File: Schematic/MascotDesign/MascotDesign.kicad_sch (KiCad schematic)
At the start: 10 parts, among them Q1 IRF540N

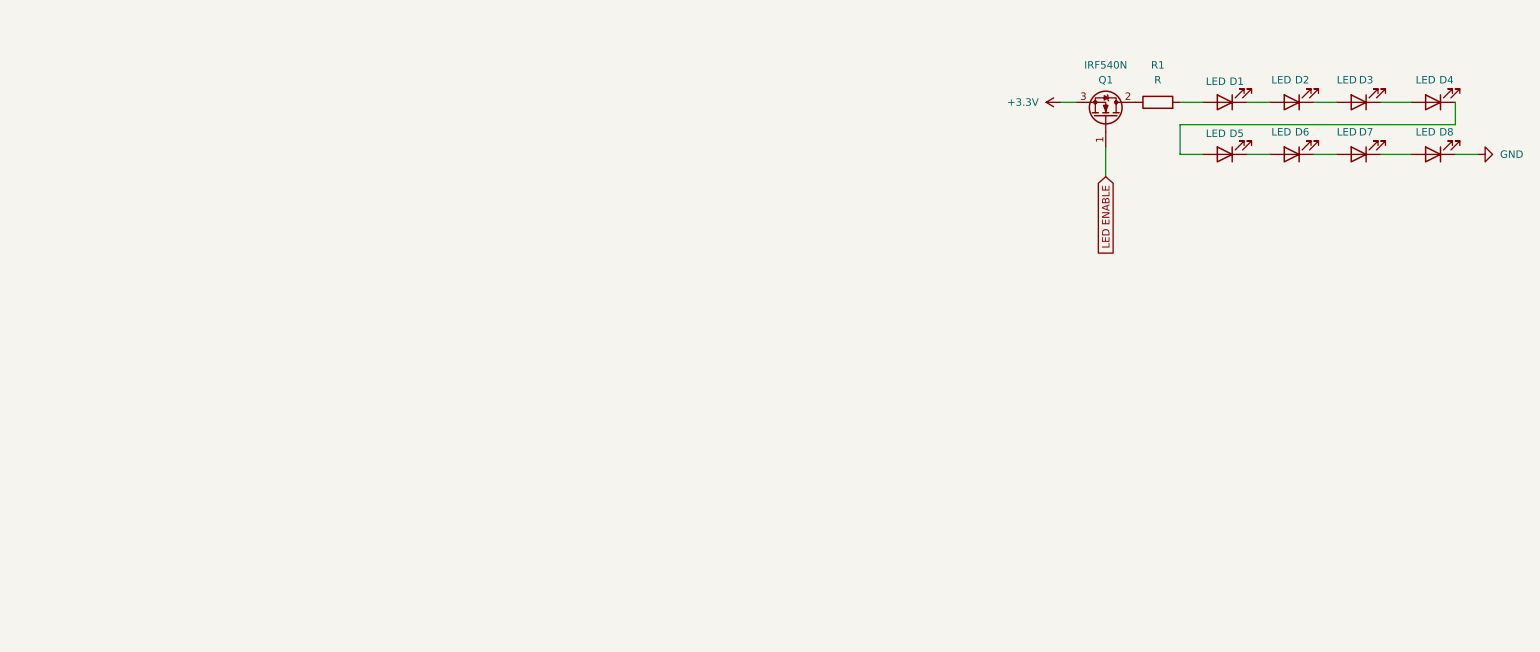
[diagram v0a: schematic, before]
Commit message: Work on schematic
create power module and LED module in the master sheet
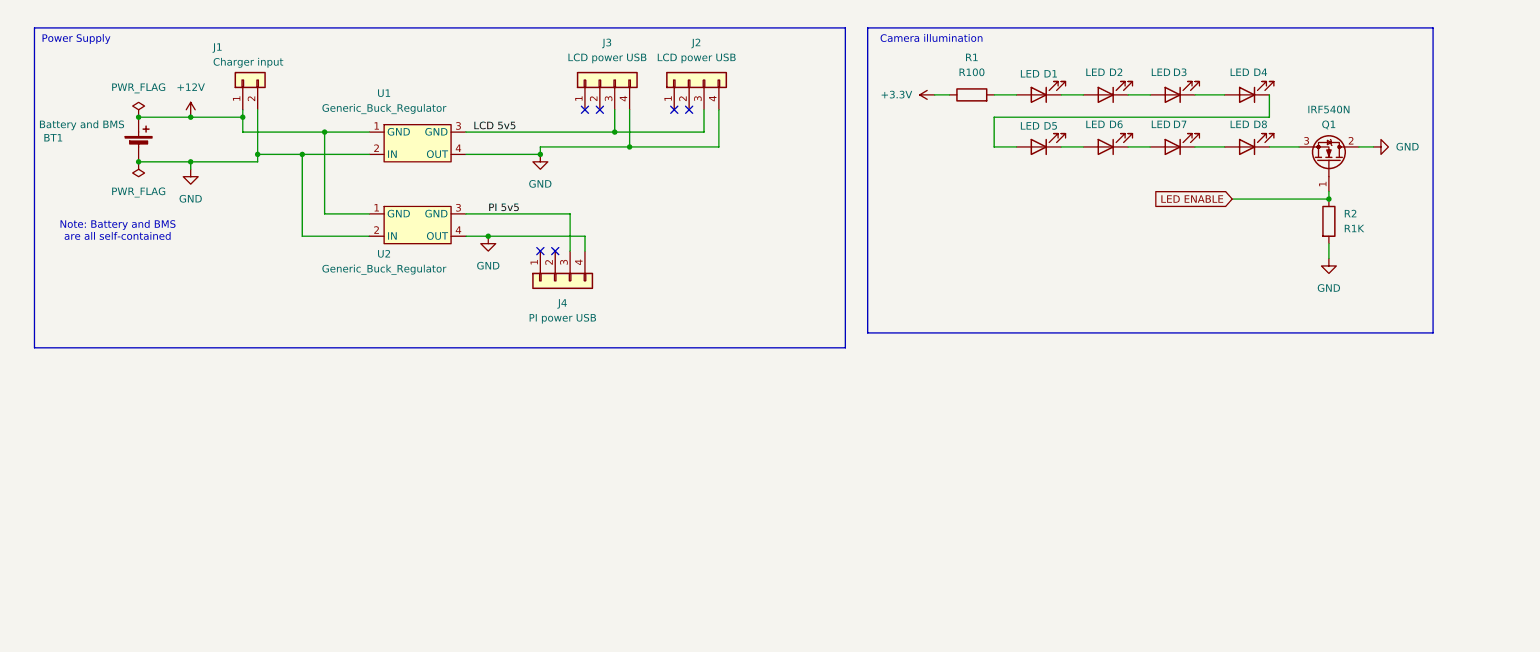
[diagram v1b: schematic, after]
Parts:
- added BT1: Battery and BMS, symbol Device:Battery_Cell
- added J1: Charger input, symbol Connector_Generic:Conn_01x02
- added J2, J3: LCD power USB, symbol Connector_Generic:Conn_01x04
- added J4: PI power USB, symbol Connector_Generic:Conn_01x04
- added R2: R1K, symbol Device:R
- added U1, U2: Generic_Buck_Regulator, My_Library:Generic Buck Regulator, symbol My_Library:Generic_Buck_Regulator
- R1: value R -> R100
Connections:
- net +3.3V: now also R1.1; no longer Q1.3 (S)
- net GND: now also Q1.2 (D), BT1.2 (-), J1.2 (Pin_2), J2.4 (Pin_4), J3.4 (Pin_4), J4.4 (Pin_4), R2.2, U1.2 (IN), U1.4 (OUT), U2.2 (IN), U2.4 (OUT); no longer D8.1 (K)
- net LED ENABLE: now also R2.1
- new net: D8.1 (K), Q1.3 (S)
- new net +12V: BT1.1 (+), J1.1 (Pin_1), U1.1 (GND), U2.1 (GND)
- new net LCD 5v5: J2.3 (Pin_3), J3.3 (Pin_3), U1.3 (GND)
- new net PI 5v5: J4.3 (Pin_3), U2.3 (GND)
- no-connect marks 0 -> 6
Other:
- note added: "Camera illumination"
- note added: "Note: Battery and BMS are all self-contained"
- note added: "Power Supply"
- moved on the sheet: D1, D2, D3, D4, D5, D6, D7, D8, Q1, R1

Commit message: organize PCB schematic into different files
so multiple people can edit different parts
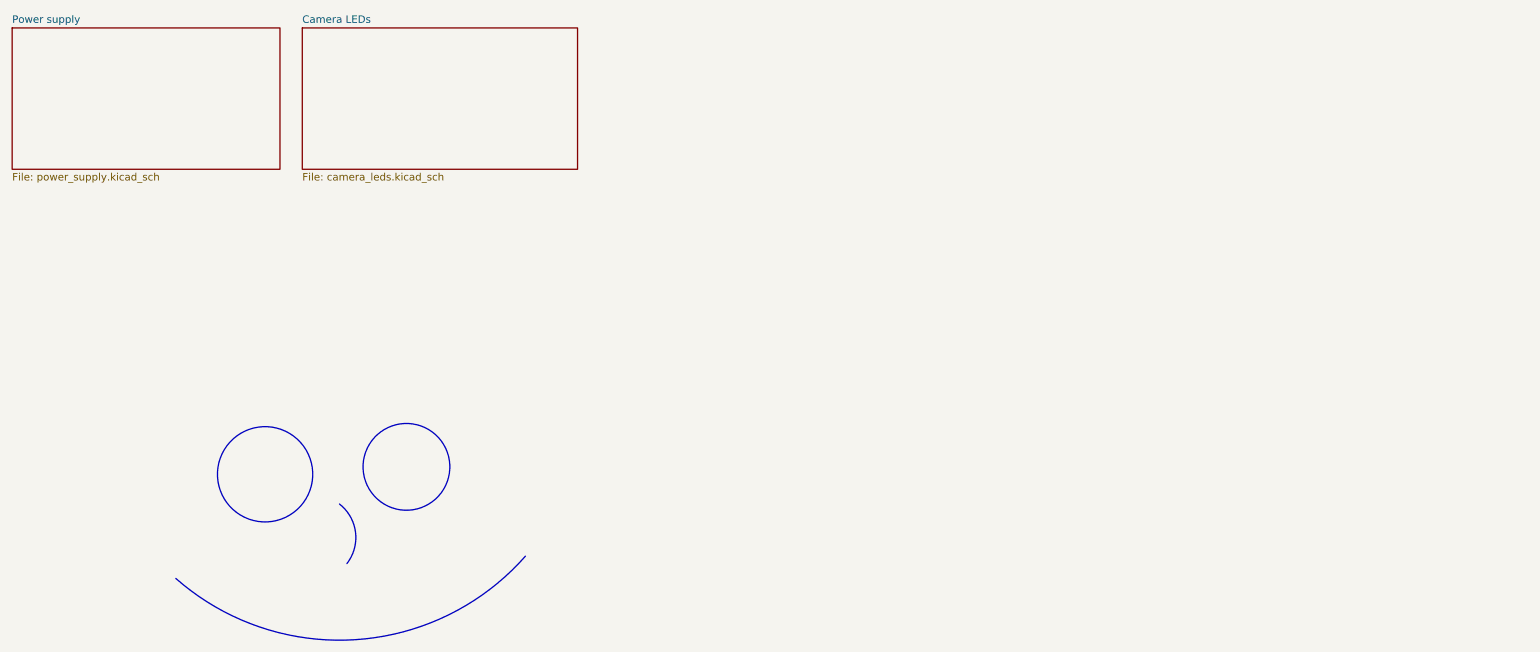
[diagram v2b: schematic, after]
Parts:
- removed BT1: Battery and BMS, symbol Device:Battery_Cell
- removed D1, D2, D3, D4, D5, D6, D7, D8: LED, symbol Device:LED
- removed J1: Charger input, symbol Connector_Generic:Conn_01x02
- removed J2, J3: LCD power USB, symbol Connector_Generic:Conn_01x04
- removed J4: PI power USB, symbol Connector_Generic:Conn_01x04
- removed Q1: IRF540N, Package_TO_SOT_THT:TO-220-3_Vertical, symbol Transistor_FET:IRF540N
- removed R1: R100, symbol Device:R
- removed R2: R1K, symbol Device:R
- removed U1, U2: Generic_Buck_Regulator, My_Library:Generic Buck Regulator, symbol My_Library:Generic_Buck_Regulator
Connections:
- no-connect marks 6 -> 0
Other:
- added sheet Camera LEDs (camera_leds.kicad_sch)
- added sheet Power supply (power_supply.kicad_sch)
- note removed: "Camera illumination"
- note removed: "Note: Battery and BMS are all self-contained"
- note removed: "Power Supply"

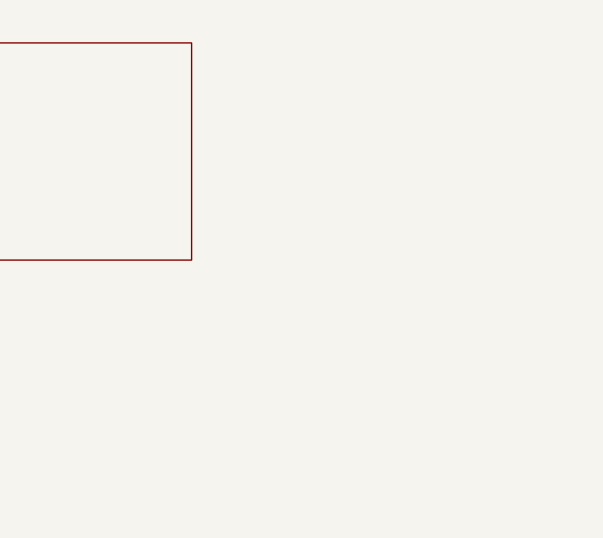
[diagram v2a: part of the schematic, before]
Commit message: Merge amplifier circuit into the rest of the schematic
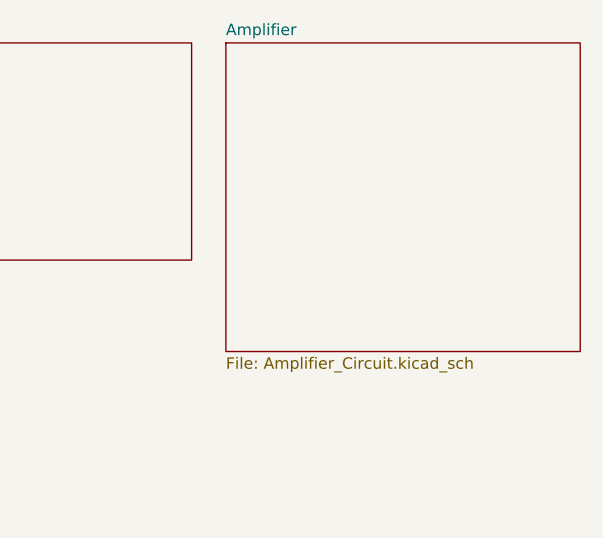
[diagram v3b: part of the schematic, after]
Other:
- added sheet Amplifier (Amplifier_Circuit.kicad_sch)
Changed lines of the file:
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@@
+	)
+	(sheet
+		(at 116.84 17.78)
+		(size 39.37 34.29)
+		(exclude_from_sim no)
+		(in_bom yes)
+		(on_board yes)
+		(dnp no)
+		(fields_autoplaced yes)
+		(stroke
+			(width 0.1524)
+			(type solid)
+		)
+		(fill
+			(color 0 0 0 0.0000)
+		)
+		(property "Sheetname" "Amplifier"
+			(at 116.84 17.0684 0)
+			(effects
+				(font
+					(size 1.27 1.27)
+				)
+				(justify left bottom)
+			)
+		)
+		(property "Sheetfile" "Amplifier_Circuit.kicad_sch"
+			(at 116.84 52.6546 0)
+			(effects
+				(font
+					(size 1.27 1.27)
+				)
+				(justify left top)
+			)
+		)
+		(instances
+			(project "MascotDesign"
+				(path "/ba045f6c-d730-41b1-992e-d77c9aee61c5"
+					(page "4")
+				)
+			)
+		)
 	)
 	(sheet

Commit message: Work on power supply schematic
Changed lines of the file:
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@@
 	(sheet
 		(at 116.84 17.78)
-		(size 39.37 34.29)
+		(size 48.26 24.13)
 		(exclude_from_sim no)
 		(in_bom yes)
@@
 		)
 		(property "Sheetfile" "Amplifier_Circuit.kicad_sch"
-			(at 116.84 52.6546 0)
+			(at 116.84 42.4946 0)
 			(effects
 				(font

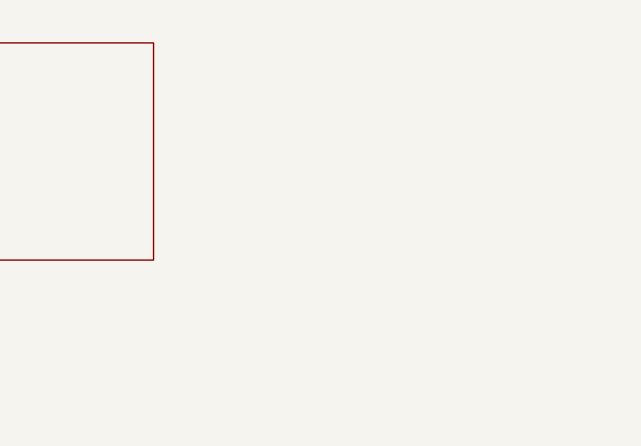
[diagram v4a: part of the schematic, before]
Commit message: Assign footprints and begin PCB layout
Need to check the ECE shop to see what parts we have on hand before we get too far into this, but still.
It's a start.
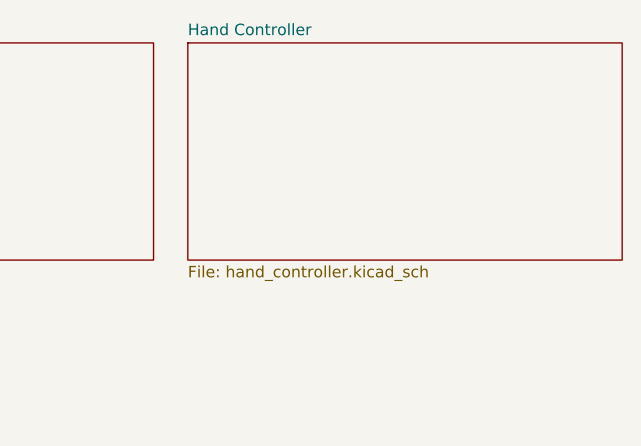
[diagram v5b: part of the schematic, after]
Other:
- added sheet Hand Controller (hand_controller.kicad_sch)
- title: (none) -> Mascot head breakout board
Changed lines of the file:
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@@
 	(generator_version "9.0")
 	(paper "A4")
+	(title_block
+		(title "Mascot head breakout board")
+		(rev "0.1")
+	)
 	(circle
 		(center 59.69 93.98)
@@
 				)
 			)
+		)
+	)
+	(sheet
+		(at 168.91 17.78)
+		(size 48.26 24.13)
+		(exclude_from_sim no)
+		(in_bom yes)
+		(on_board yes)
+		(dnp no)
+		(fields_autoplaced yes)
+		(stroke
+			(width 0.1524)
+			(type solid)
+		)
+		(fill
+			(color 0 0 0 0.0000)
+		)
+		(property "Sheetname" "Hand Controller"
+			(at 168.91 17.0684 0)
+			(effects
+				(font
+					(size 1.27 1.27)
+				)
+				(justify left bottom)
+			)
+		)
+		(property "Sheetfile" "hand_controller.kicad_sch"
+			(at 168.91 42.4946 0)
+			(effects
+				(font
+					(size 1.27 1.27)
+				)
+				(justify left top)
+			)
+		)
+		(instances
+			(project "MascotDesign"
+				(path "/ba045f6c-d730-41b1-992e-d77c9aee61c5"
+					(page "5")
+				)
+			)

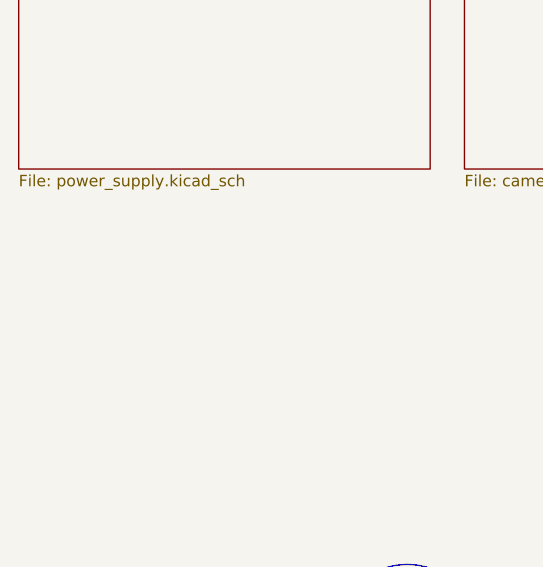
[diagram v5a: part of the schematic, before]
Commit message: update PCB and mounting brackets
give PCB the correct footprints for the parts we have and add more mounting brackets for the 3D model
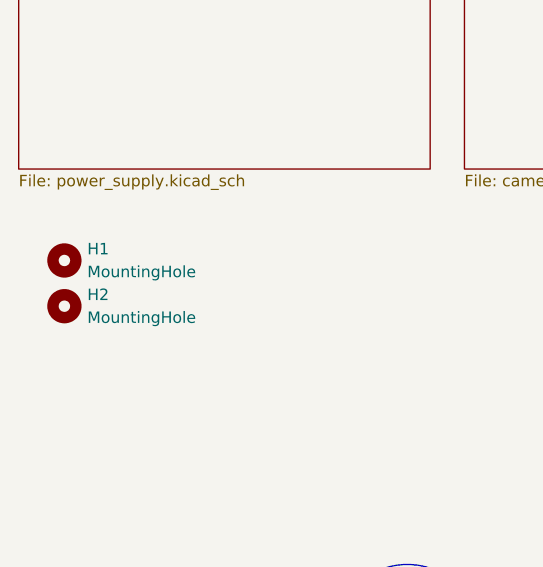
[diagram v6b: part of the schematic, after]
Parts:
- added H1, H2: MountingHole, MountingHole:MountingHole_2.2mm_M2, symbol Mechanical:MountingHole
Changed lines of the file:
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@@
+		)
+	)
+	(symbol
+		(lib_id "Mechanical:MountingHole")
+		(at 21.59 52.07 0)
+		(unit 1)
+		(exclude_from_sim no)
+		(in_bom no)
+		(on_board yes)
+		(dnp no)
+		(fields_autoplaced yes)
+		(property "Reference" "H1"
+			(at 24.13 50.7999 0)
+			(effects
+				(font
+					(size 1.27 1.27)
+				)
+				(justify left)
+			)
+		)
+		(property "Value" "MountingHole"
+			(at 24.13 53.3399 0)
+			(effects
+				(font
+					(size 1.27 1.27)
+				)
+				(justify left)
+			)
+		)
+		(property "Footprint" "MountingHole:MountingHole_2.2mm_M2"
+			(at 21.59 52.07 0)
+			(effects
+				(font
+					(size 1.27 1.27)
+				)
+				(hide yes)
+			)
+		)
+		(property "Datasheet" "~"
+			(at 21.59 52.07 0)
+			(effects
+				(font
+					(size 1.27 1.27)
+				)
+				(hide yes)
+			)
+		)
+		(property "Description" "Mounting Hole without connection"
+			(at 21.59 52.07 0)
+			(effects
+				(font
+					(size 1.27 1.27)
+				)
+				(hide yes)
+			)
+		)
+		(instances
+			(project ""
+				(path "/ba045f6c-d730-41b1-992e-d77c9aee61c5"
+					(reference "H1")
+					(unit 1)
+				)
+			)
+		)
+	)
+	(symbol
+		(lib_id "Mechanical:MountingHole")
+		(at 21.59 57.15 0)
+		(unit 1)
+		(exclude_from_sim no)
+		(in_bom no)
+		(on_board yes)
+		(dnp no)
+		(fields_autoplaced yes)
+		(property "Reference" "H2"
+			(at 24.13 55.8799 0)
+			(effects
+				(font
+					(size 1.27 1.27)
+				)
+				(justify left)
+			)
+		)
+		(property "Value" "MountingHole"
+			(at 24.13 58.4199 0)
+			(effects
+				(font
+					(size 1.27 1.27)
+				)
+				(justify left)
+			)
+		)
+		(property "Footprint" "MountingHole:MountingHole_2.2mm_M2"
+			(at 21.59 57.15 0)
+			(effects
+				(font
+					(size 1.27 1.27)
+				)
+				(hide yes)
+			)
+		)
+		(property "Datasheet" "~"
+			(at 21.59 57.15 0)
+			(effects
+				(font
+					(size 1.27 1.27)
+				)
+				(hide yes)
+			)
+		)
+		(property "Description" "Mounting Hole without connection"
+			(at 21.59 57.15 0)
+			(effects
+				(font
+					(size 1.27 1.27)
+				)
+				(hide yes)
+			)
+		)
+		(instances
+			(project "MascotDesign"
+				(path "/ba045f6c-d730-41b1-992e-d77c9aee61c5"
+					(reference "H2")
+					(unit 1)
+				)
+			)
 		)
 	)
